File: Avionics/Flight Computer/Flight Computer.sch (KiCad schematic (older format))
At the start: 13 parts

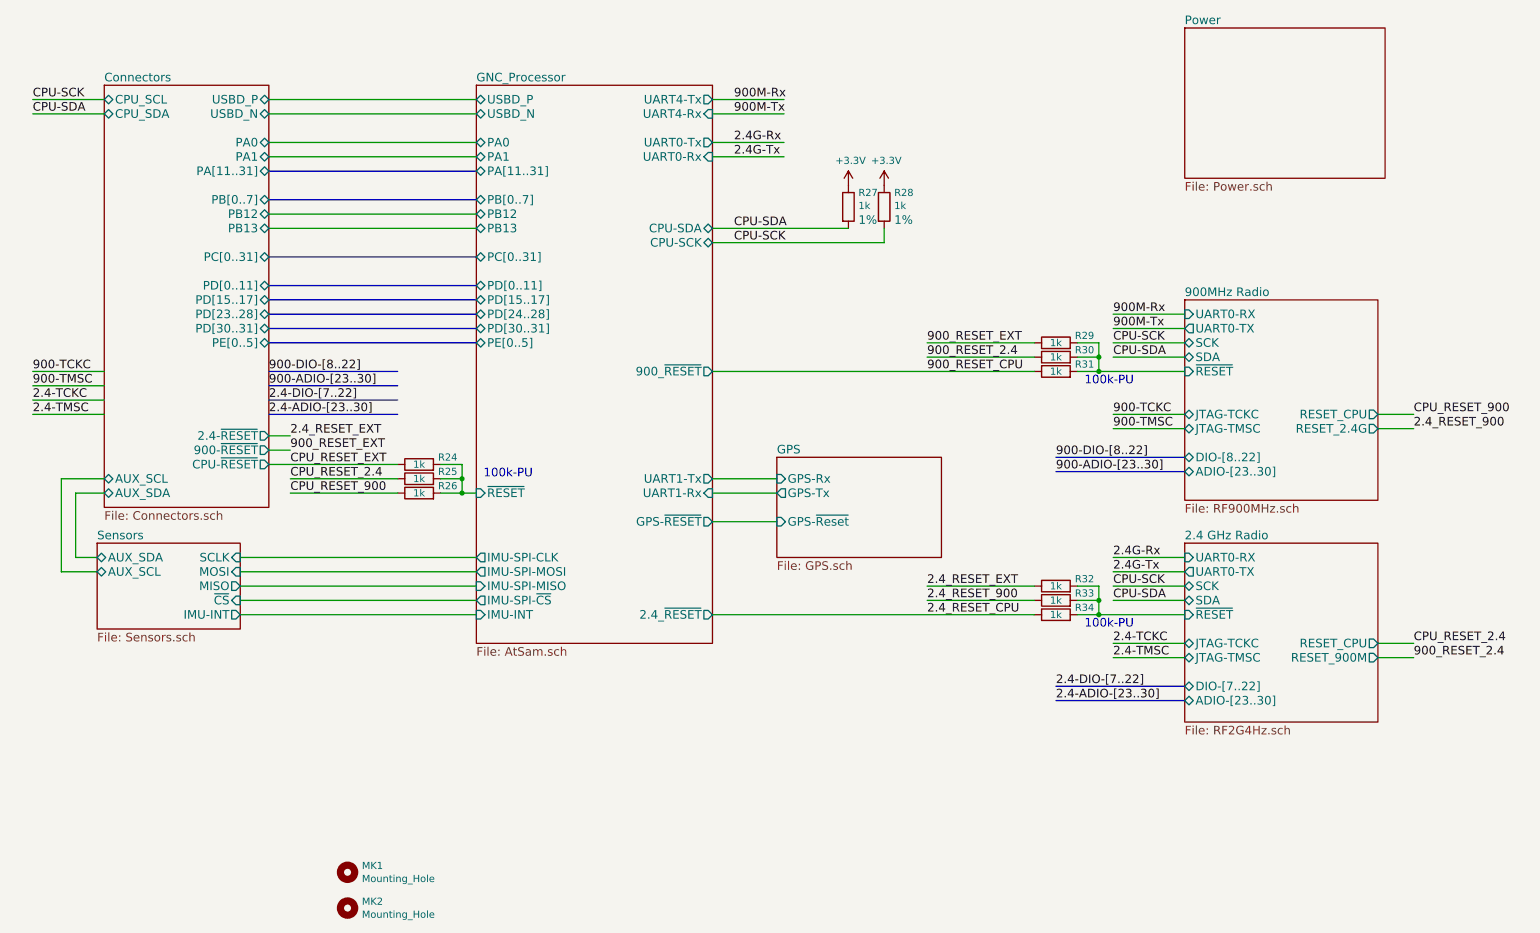
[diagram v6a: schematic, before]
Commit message: Fixed missing connections and did more layout
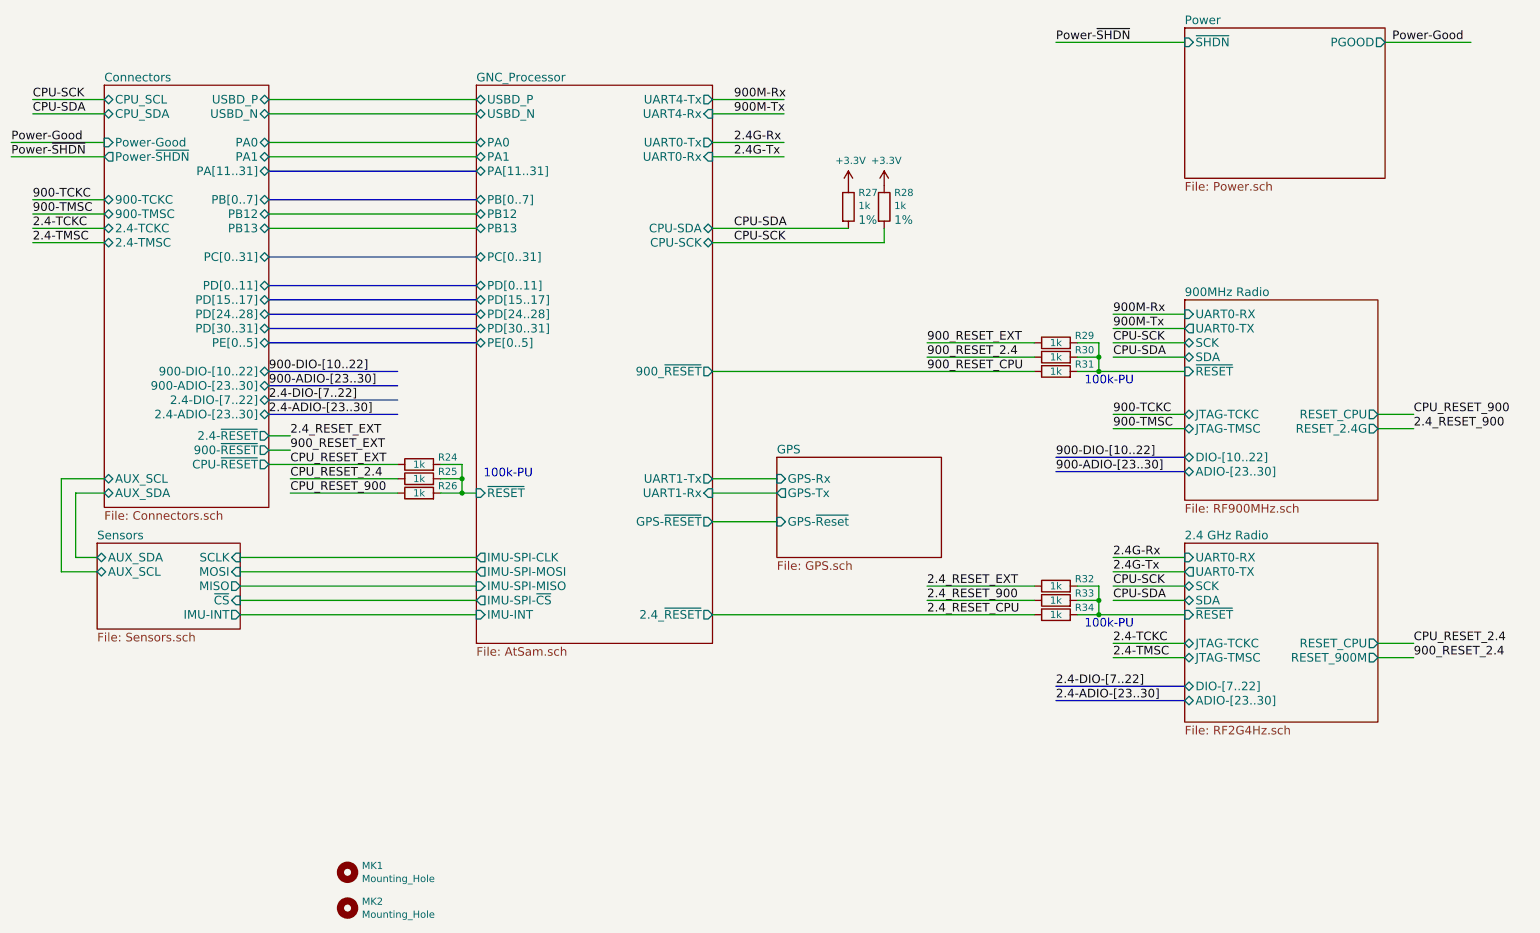
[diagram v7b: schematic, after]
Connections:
- net labels added: 900-DIO-[10..22], Power-Good, Power-~SHDN~
- net labels removed: 900-DIO-[8..22]
- wire segments 78 -> 76
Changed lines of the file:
@@
 F6 "JTAG-TMSC" B L 8750 3900 60
 F7 "JTAG-TCKC" B L 8750 3800 60
-F8 "DIO-[8..22]" B L 8750 4100 60
+F8 "DIO-[10..22]" B L 8750 4100 60
 F9 "RESET_2.4G" O R 10100 3900 60
 F10 "RESET_CPU" O R 10100 3800 60
@@
 F0 "Power" 60
 F1 "Power.sch" 60
+F2 "~SHDN" I L 8750 1200 60
+F3 "PGOOD" O R 10150 1200 60
 $EndSheet
 $Sheet
@@
 F8 "PD[0..11]" B R 2350 2900 60
 F9 "PD[15..17]" B R 2350 3000 60
-F10 "PD[23..28]" B R 2350 3100 60
+F10 "PD[24..28]" B R 2350 3100 60
 F11 "PE[0..5]" B R 2350 3300 60
 F12 "PD[30..31]" B R 2350 3200 60
@@
 F21 "PB13" B R 2350 2500 60
 F22 "PB12" B R 2350 2400 60
+F23 "900-TCKC" B L 1200 2300 60
+F24 "900-TMSC" B L 1200 2400 60
+F25 "2.4-TCKC" B L 1200 2500 60
+F26 "2.4-TMSC" B L 1200 2600 60
+F27 "900-DIO-[10..22]" B R 2350 3500 60
+F28 "900-ADIO-[23..30]" B R 2350 3600 60
+F29 "2.4-DIO-[7..22]" B R 2350 3700 60
+F30 "2.4-ADIO-[23..30]" B R 2350 3800 60
+F31 "Power-Good" I L 1200 1900 60
+F32 "Power-~SHDN" O L 1200 2000 60
 $EndSheet
 Text Label 5600 1900 0    60   ~ 0
@@
 900-ADIO-[23..30]
 Text Label 7850 4100 0    60   ~ 0
-900-DIO-[8..22]
+900-DIO-[10..22]
 Text Label 6950 5200 0    60   ~ 0
 2.4_RESET_CPU
@@
 Text Label 6950 3500 0    60   ~ 0
 900_RESET_CPU
-Text Label 700  3500 0    60   ~ 0
+Text Label 700  2300 0    60   ~ 0
 900-TCKC
-Text Label 700  3600 0    60   ~ 0
+Text Label 700  2400 0    60   ~ 0
 900-TMSC
 Text Label 2350 3600 0    60   ~ 0
 900-ADIO-[23..30]
 Text Label 2350 3500 0    60   ~ 0
-900-DIO-[8..22]
-Text Label 700  3700 0    60   ~ 0
+900-DIO-[10..22]
+Text Label 700  2500 0    60   ~ 0
 2.4-TCKC
-Text Label 700  3800 0    60   ~ 0
+Text Label 700  2600 0    60   ~ 0
 2.4-TMSC
 Text Label 2350 3800 0    60   ~ 0
@@
 	6650 2600 6650 2500
 Wire Wire Line
-	3550 4350 3700 4350
-Wire Wire Line
-	3700 4350 3800 4350
+	3550 4350 3800 4350
 Wire Wire Line
 	3550 4250 3700 4250
 Wire Wire Line
-	3700 4150 3700 4250
-Wire Wire Line
-	3700 4250 3700 4350
+	3700 4150 3700 4350
 Connection ~ 3700 4350
 Wire Wire Line
@@
 	10100 5500 10350 5500
 Wire Wire Line
-	8000 5200 8150 5200
-Wire Wire Line
-	8150 5200 8750 5200
+	8000 5200 8750 5200
 Wire Wire Line
 	8000 5100 8150 5100
 Wire Wire Line
-	8150 5000 8150 5100
-Wire Wire Line
-	8150 5100 8150 5200
+	8150 5000 8150 5200
 Connection ~ 8150 5200
 Wire Wire Line
@@
 	7850 4200 8750 4200
 Wire Wire Line
-	8000 3500 8150 3500
-Wire Wire Line
-	8150 3500 8750 3500
+	8000 3500 8750 3500
 Wire Wire Line
 	8000 3400 8150 3400
 Wire Wire Line
-	8150 3300 8150 3400
-Wire Wire Line
-	8150 3400 8150 3500
+	8150 3300 8150 3500
 Connection ~ 8150 3500
 Wire Wire Line
@@
 	900  4900 1150 4900
 Wire Wire Line
-	1200 3500 700  3500
-Wire Wire Line
-	1200 3600 700  3600
+	1200 2300 700  2300
+Wire Wire Line
+	1200 2400 700  2400
 Wire Bus Line
 	2350 3500 3250 3500
@@
 	2350 3600 3250 3600
 Wire Wire Line
-	1200 3700 700  3700
+	1200 2500 700  2500
 Wire Bus Line
 	2350 3700 3250 3700
@@
 	2350 3800 3250 3800
 Wire Wire Line
-	700  3800 1200 3800
+	700  2600 1200 2600
 Wire Bus Line
 	2350 3300 3800 3300
@@
 Wire Wire Line
 	3800 2500 2350 2500
+Wire Wire Line
+	8750 1200 7850 1200
+Text Label 7850 1200 0    60   ~ 0
+Power-~SHDN~
+Wire Wire Line
+	10150 1200 10750 1200
+Text Label 10200 1200 0    60   ~ 0
+Power-Good
+Wire Wire Line
+	1200 2000 550  2000
+Text Label 550  2000 0    60   ~ 0
+Power-~SHDN~
+Wire Wire Line
+	550  1900 1200 1900
+Text Label 550  1900 0    60   ~ 0
+Power-Good
 $EndSCHEMATC

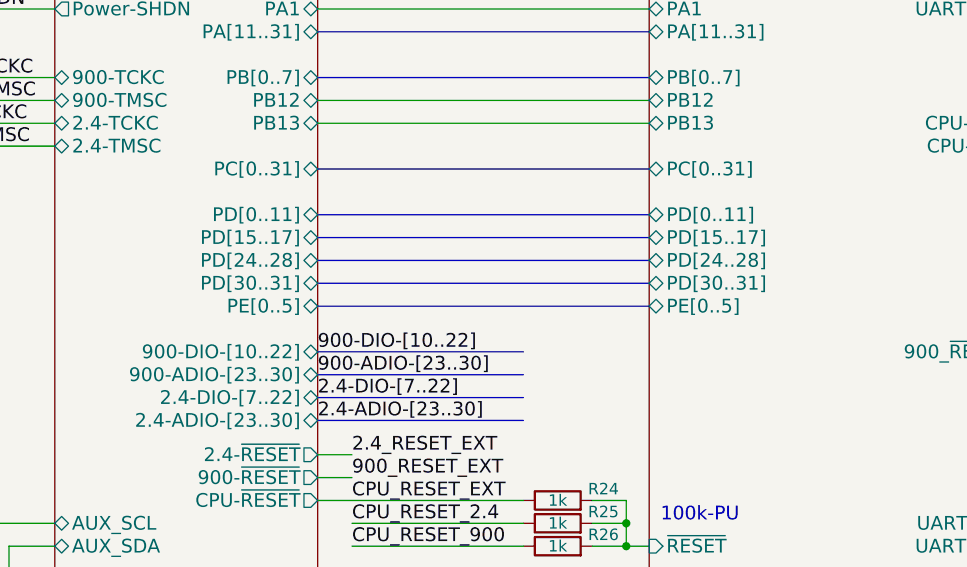
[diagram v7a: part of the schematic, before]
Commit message: Some more pin swapping and routing of signals. Placed reset pullup resistors.
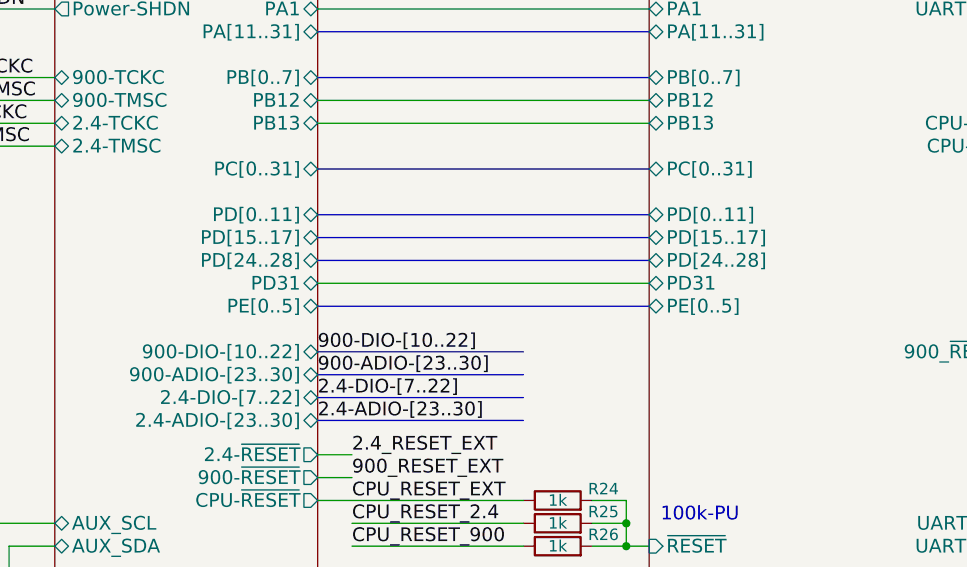
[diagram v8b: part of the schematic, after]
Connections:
- wire segments 76 -> 77
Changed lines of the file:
@@
 F28 "900_~RESET" O R 5450 3500 60
 F29 "2.4_~RESET" O R 5450 5200 60
-F30 "PD[30..31]" B L 3800 3200 60
-F31 "GPS-~RESET" O R 5450 4550 60
-F32 "PD[24..28]" B L 3800 3100 60
+F30 "GPS-~RESET" O R 5450 4550 60
+F31 "PD[24..28]" B L 3800 3100 60
+F32 "PD31" B L 3800 3200 60
 $EndSheet
 $Sheet
@@
 F10 "PD[24..28]" B R 2350 3100 60
 F11 "PE[0..5]" B R 2350 3300 60
-F12 "PD[30..31]" B R 2350 3200 60
+F12 "PD31" B R 2350 3200 60
 F13 "AUX_SDA" B L 1200 4350 60
 F14 "AUX_SCL" B L 1200 4250 60
@@
 $EndComp
 $Comp
-L +3.3V #PWR01
+L +3.3V #PWR2
 U 1 1 58BFF81C
 P 6650 2200
-F 0 "#PWR01" H 4950 -300 50  0001 C CNN
+F 0 "#PWR2" H 4950 -300 50  0001 C CNN
 F 1 "+3.3V" H 6665 2373 50  0000 C CNN
 F 2 "" H 4950 -150 50  0001 C CNN
@@
 $EndComp
 $Comp
-L +3.3V #PWR02
+L +3.3V #PWR1
 U 1 1 58BFF8E0
 P 6400 2200
-F 0 "#PWR02" H 4700 -300 50  0001 C CNN
+F 0 "#PWR1" H 4700 -300 50  0001 C CNN
 F 1 "+3.3V" H 6415 2373 50  0000 C CNN
 F 2 "" H 4700 -150 50  0001 C CNN
@@
 	2350 3300 3800 3300
 Wire Bus Line
-	3800 3200 2350 3200
-Wire Bus Line
 	2350 3100 3800 3100
 Wire Bus Line
@@
 Text Label 550  1900 0    60   ~ 0
 Power-Good
+Wire Wire Line
+	3800 3200 2350 3200
 $EndSCHEMATC
